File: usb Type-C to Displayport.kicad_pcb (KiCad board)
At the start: 4 copper layers, 50 x 25.9 mm, 23 parts, among them CN1 HYC16-DP20-178, J1 USB_C_Receptacle, U1 VL103-Q3, U2 W25Q16BVSSIG

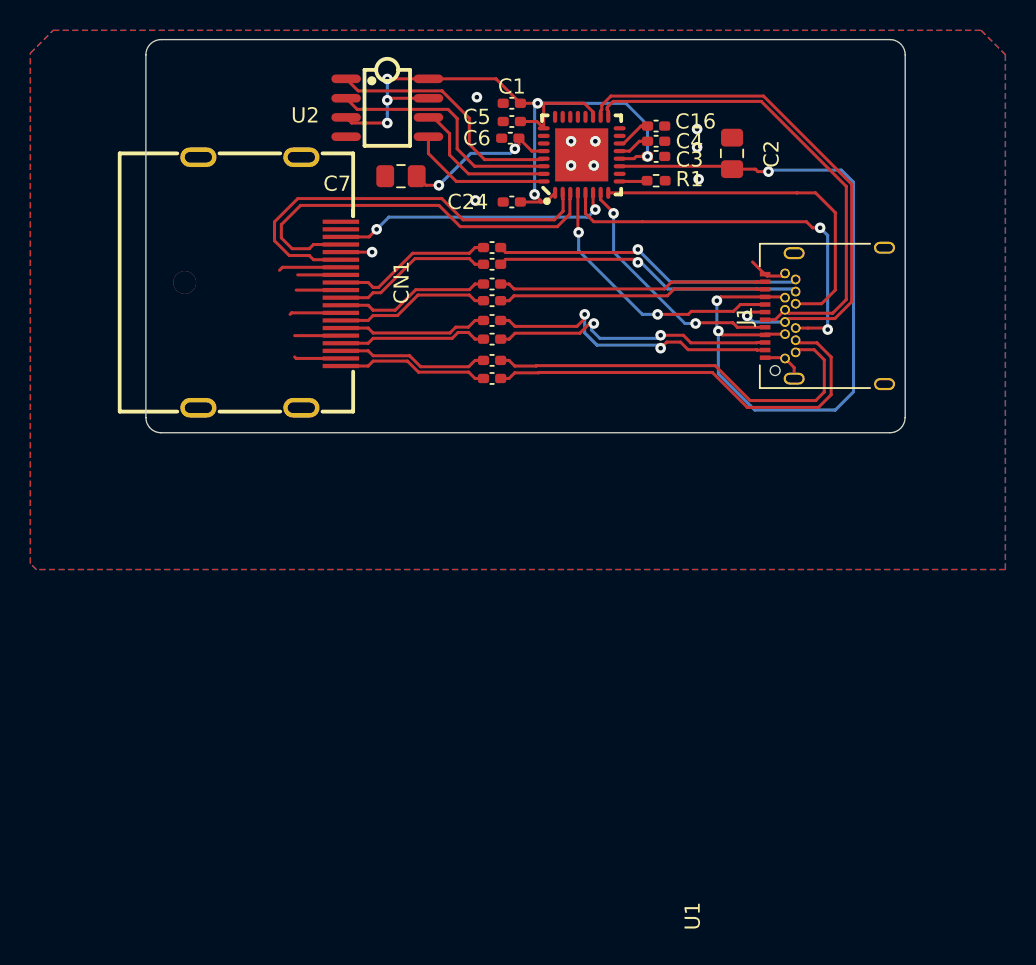
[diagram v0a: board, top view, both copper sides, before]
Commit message: 0.2
Removed SPI chip, fixed CC lines being reversed, made pcb smaller, added mounting holes
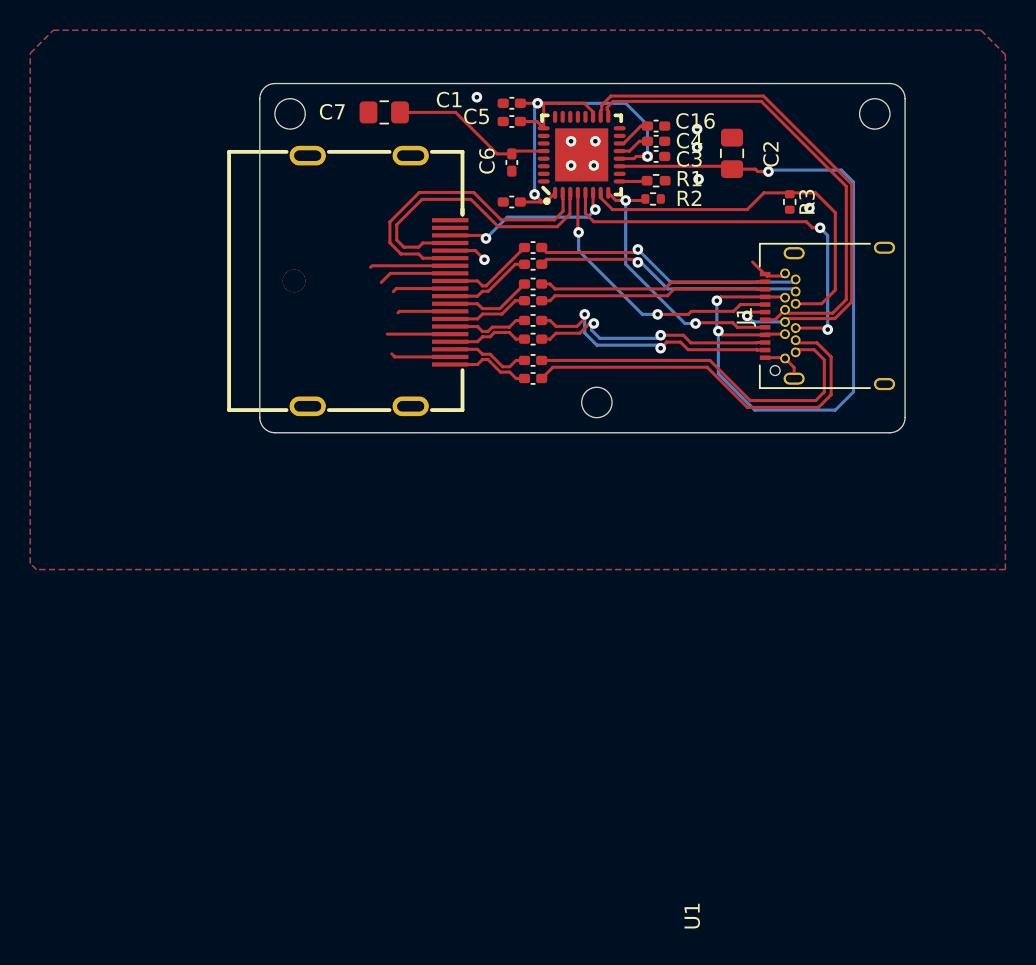
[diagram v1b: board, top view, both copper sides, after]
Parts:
- removed U2: W25Q16BVSSIG, da:SOIC-8_L5.0-W4.0-P1.27-LS6.0-BL
- added R2: 5.1K, Resistor_SMD:R_0402_1005Metric, F.Cu at (103.7, 59.3)
- added R3: 5.1K, Resistor_SMD:R_0402_1005Metric, F.Cu at (112.7, 59.5)
- R1: value 20.5k -> 243K
- moved CN1 7.20 mm to (85.7, 64.7)
- moved C7 4.34 mm to (86.0, 53.6)
- moved C10 2.70 mm to (95.8, 68.5)
- moved C11 2.70 mm to (95.8, 67.3)
- moved C12 2.70 mm to (95.8, 66.0)
- moved C13 2.70 mm to (95.8, 64.9)
- moved C14 2.70 mm to (95.8, 63.6)
- moved C15 2.70 mm to (95.8, 62.5)
- moved C8 2.70 mm to (95.8, 71.1)
- moved C9 2.70 mm to (95.8, 69.9)
- moved G*** 2.15 mm to (108.2, 55.1)
- moved C6 1.60 mm to (94.4, 56.9), turned to -90 degrees
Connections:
- U1 pad 29: SPI_CS -> unconnected-(U1-SPI_CS_-Pad29)
- U1 pad 30: SPI_DO -> unconnected-(U1-SPI_Q-Pad30)
- U1 pad 31: SCLK -> unconnected-(U1-SPI_CLK-Pad31)
- U1 pad 32: SPI_DI -> unconnected-(U1-SPI_D-Pad32)
- U1 pad 7: CC1 -> CC2
- U1 pad 8: CC2 -> CC1
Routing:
- net +3.3V: track 47.7 -> 29.8 mm, vias 6 -> 3
- net SPI_CS: track 16.2 -> 0.00 mm
- net SPI_DO: track 16.0 -> 0.00 mm
- net SCLK: track 9.95 -> 0.00 mm
- net SPI_DI: track 9.46 -> 0.00 mm
- net AUX-: track 27.1 -> 19.4 mm
- net AUX+: track 27.8 -> 20.2 mm
- net HPD: track 18.7 -> 11.6 mm
- net GND: track 27.0 -> 33.4 mm
- net DP_LANE3-: track 10.6 -> 5.76 mm
- net DP_LANE2-: track 10.2 -> 5.39 mm
- net DP_LANE3+: track 10.6 -> 6.07 mm
- net DP_LANE1+: track 9.87 -> 5.32 mm
- net DP_LANE2+: track 10.2 -> 5.70 mm
- net DP_LANE1-: track 9.87 -> 5.32 mm
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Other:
- board size 50 x 25.9 mm -> 42.5 x 23 mm

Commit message: Changed IC to vl100 q3
Changed ic to vl100 q3 (i found it cheaper and it's pin compatible, added Crystal)
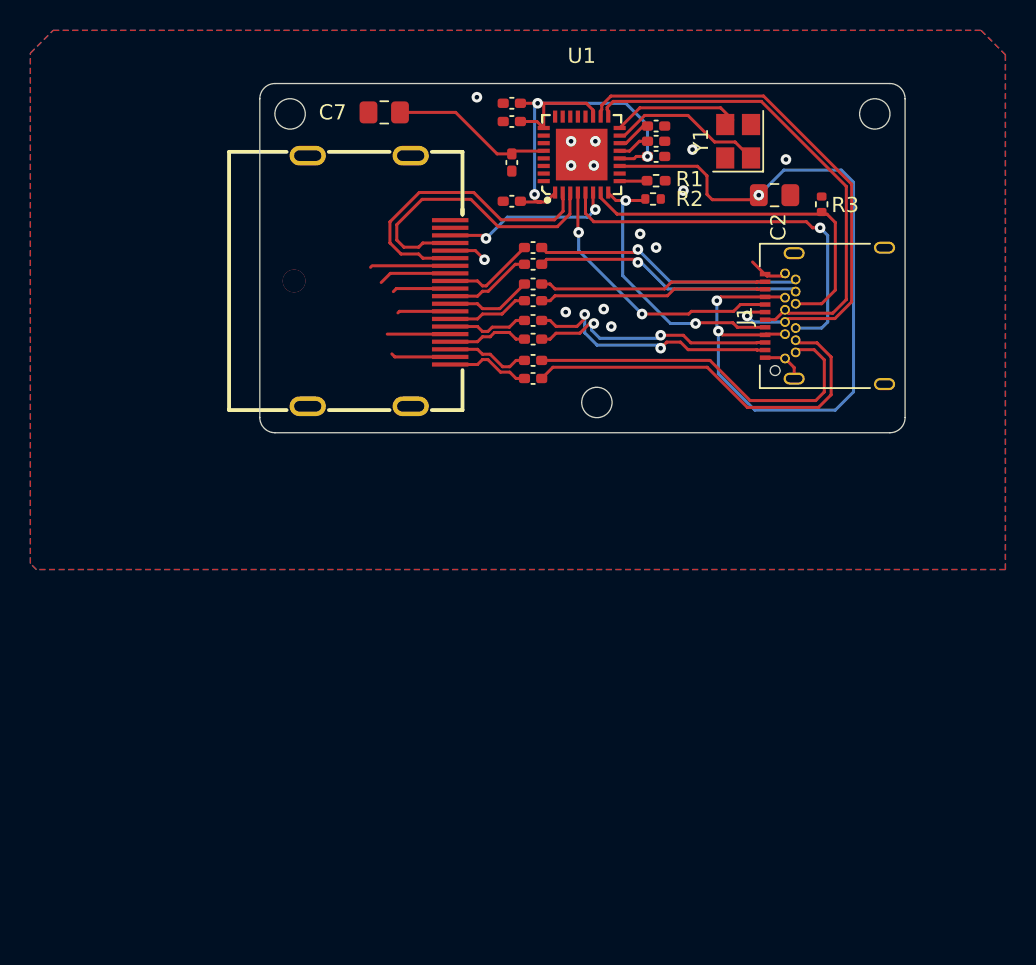
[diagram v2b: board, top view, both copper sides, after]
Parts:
- removed C24: 100nF, Capacitor_SMD:C_0402_1005Metric_Pad0.74x0.62mm_HandSolder
- added C17: 100nF, Capacitor_SMD:C_0402_1005Metric_Pad0.74x0.62mm_HandSolder, F.Cu at (94.4, 59.5)
- added Y1: Crystal_GND24, Crystal:Crystal_SMD_3225-4Pin_3.2x2.5mm, F.Cu at (109.3, 55.5)
- R1: value 243K -> 20.5K
- U1: value VL103-Q3 -> VL100-Q3; footprint da:QFN-32_L5.0-W5.0-P0.50-TL-EP3.5 -> da:QFN-32_L5.0-W5.0-P0.50-BL-EP3.4
- moved C2 3.92 mm to (111.7, 59.0), turned to 0 degrees
- moved R3 2.11 mm to (114.8, 59.6), turned to 90 degrees
- moved G*** 1.10 mm to (107.1, 55.2)
- turned U1 to 0 degrees
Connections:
- U1 pad 15: unconnected-(U1-GPIO11-Pad15) -> Net-(U1-OSCXI)
- U1 pad 16: unconnected-(U1-GPIO10-Pad16) -> Net-(U1-OSCXO)
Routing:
- net Net-(U1-OSCXI): track 0.00 -> 10.4 mm
- net Net-(U1-OSCXO): track 0.00 -> 8.33 mm
- net VBUS: track 54.1 -> 56.3 mm
- net CC2: track 25.2 -> 23.9 mm
- net CC1: track 17.8 -> 18.6 mm
- net SBU2: track 26.3 -> 25.9 mm, vias 2 -> 1
- net GND: vias 10 -> 14

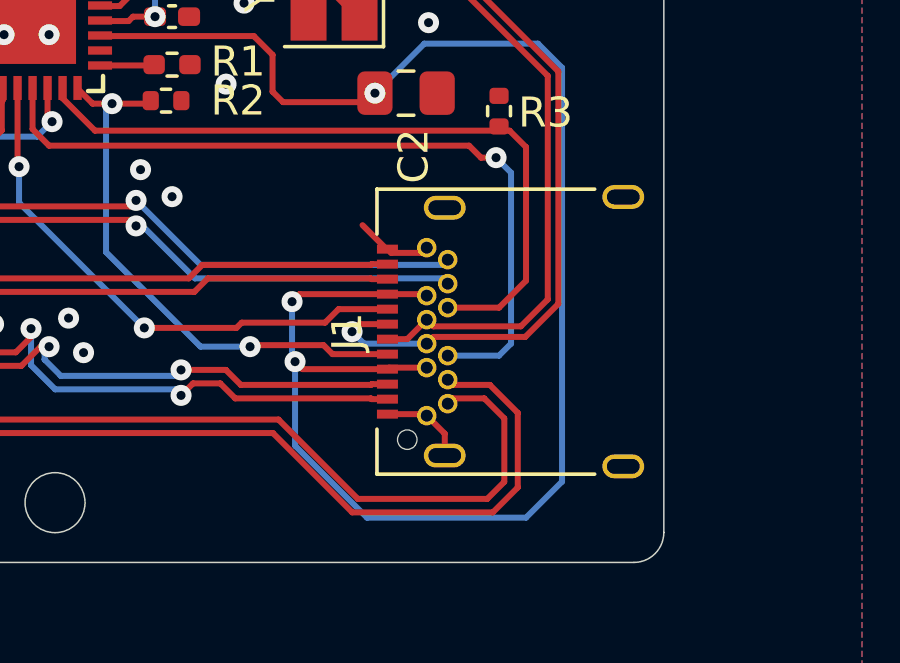
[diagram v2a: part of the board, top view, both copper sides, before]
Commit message: Fixed usb footprint
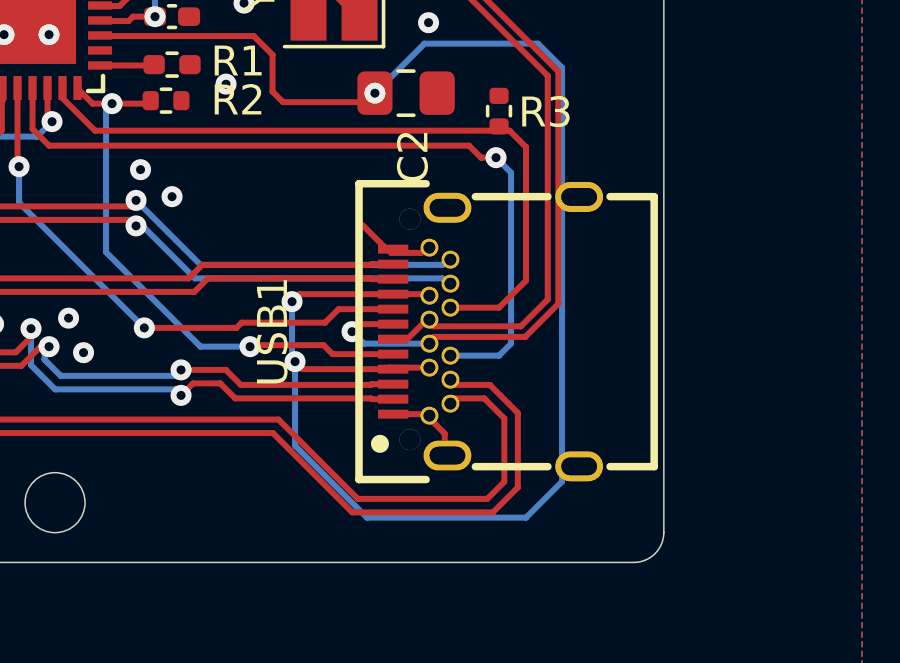
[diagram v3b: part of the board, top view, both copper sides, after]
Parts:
- removed J1: USB_C_Receptacle, Connector_USB:USB_C_Receptacle_Amphenol_12401548E4-2A
- added USB1: TYPEC-324-BCP24, da:USB-C-SMD_TYPEC-324-BCP24, F.Cu at (114.4, 67.0)
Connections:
- C10 pad 1: /TX1- -> TX1-
- C11 pad 1: /TX1+ -> TX1+
- C12 pad 1: /RX2- -> RX2-
- C13 pad 1: /RX2+ -> RX2+
- C14 pad 1: /TX2- -> TX2-
- C15 pad 1: /TX2+ -> TX2+
- C8 pad 1: /RX1- -> RX1-
- C9 pad 1: /RX1+ -> RX1+
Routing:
- net RX1-: track 0.00 -> 26.1 mm
- net /RX1-: track 26.1 -> 0.00 mm
- net RX1+: track 0.00 -> 24.3 mm
- net /RX1+: track 24.3 -> 0.00 mm
- net TX2+: track 0.00 -> 17.9 mm, vias 0 -> 1
- net /TX2+: track 17.9 -> 0.00 mm, vias 1 -> 0
- net TX2-: track 0.00 -> 17.7 mm, vias 0 -> 1
- net /TX2-: track 17.7 -> 0.00 mm, vias 1 -> 0
- net TX1+: track 0.00 -> 17.4 mm, vias 0 -> 2
- net /TX1+: track 17.4 -> 0.00 mm, vias 2 -> 0
- net TX1-: track 0.00 -> 16.3 mm, vias 0 -> 2
- net /TX1-: track 16.3 -> 0.00 mm, vias 2 -> 0
- net RX2-: track 0.00 -> 15.0 mm
- net /RX2-: track 15.0 -> 0.00 mm
- net RX2+: track 0.00 -> 15.0 mm
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
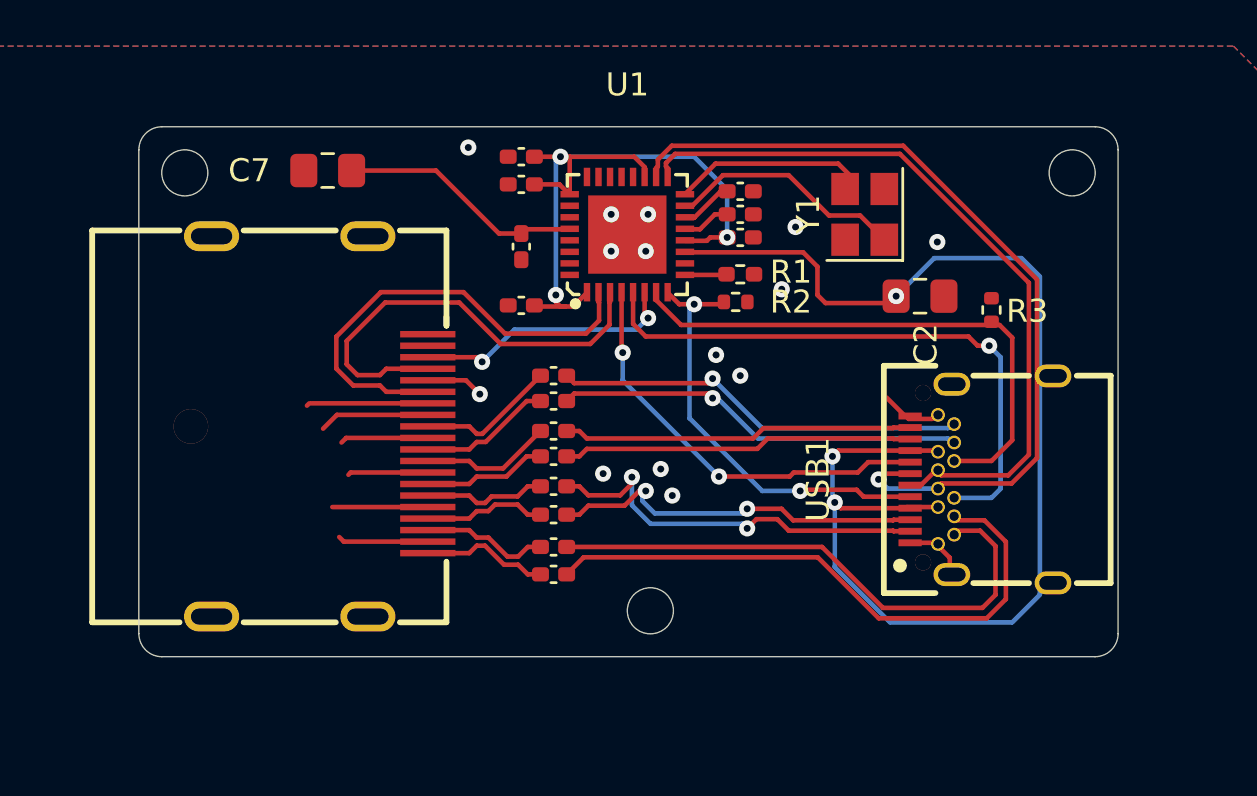
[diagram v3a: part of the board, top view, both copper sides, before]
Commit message: Fixed DP lines
Fixed wrong USB lines to DP lines, fixed differential pairs not length matched, length matched all 4 pairs
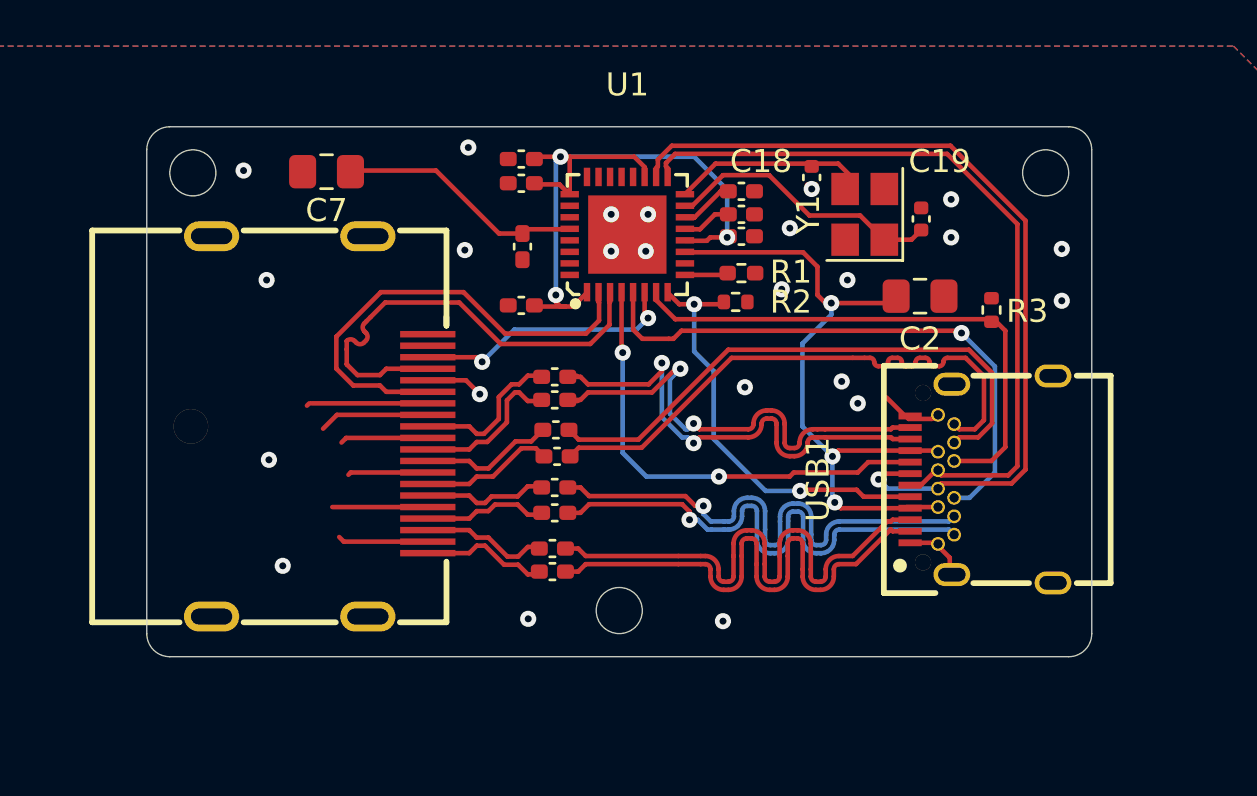
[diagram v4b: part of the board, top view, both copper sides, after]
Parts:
- added C18: 20pF, Capacitor_SMD:C_0402_1005Metric, F.Cu at (107.0, 53.9)
- added C19: 20pF, Capacitor_SMD:C_0402_1005Metric, F.Cu at (111.8, 55.7)
- Y1: value Crystal_GND24 -> 24Mhz
- moved G*** 1.61 mm to (105.5, 54.9)
- moved C10 1.18 mm to (95.8, 67.3)
- moved C12 1.15 mm to (95.9, 64.8)
- moved C11 1.15 mm to (95.8, 68.5)
- moved C8 1.12 mm to (95.8, 70.0)
- moved C13 1.11 mm to (96.0, 66.0)
- moved C9 1.07 mm to (95.8, 71.0)
- moved C14 1.05 mm to (95.8, 62.5)
- moved C15 1.05 mm to (95.8, 63.5)
- moved C1 0.10 mm to (94.4, 53.1)
- moved R1 0.07 mm to (104.0, 58.0)
- moved C3 0.07 mm to (104.0, 56.5)
- moved C7 0.07 mm to (86.0, 53.6)
- moved C5 0.05 mm to (94.4, 54.1)
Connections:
- C10 pad 1: TX1- -> RX1-
- C11 pad 1: TX1+ -> RX1+
- C12 pad 1: RX2- -> TX2-
- C13 pad 1: RX2+ -> TX2+
- C14 pad 1: TX2- -> RX2-
- C15 pad 1: TX2+ -> RX2+
- C8 pad 1: RX1- -> TX1-
- C9 pad 1: RX1+ -> TX1+
- CN1 pad 1: DP_LANE0- -> DP_LANE0+
- CN1 pad 10: DP_LANE3- -> DP_LANE3+
- CN1 pad 12: DP_LANE3+ -> DP_LANE3-
- CN1 pad 3: DP_LANE0+ -> DP_LANE0-
- CN1 pad 4: DP_LANE1- -> DP_LANE1+
- CN1 pad 6: DP_LANE1+ -> DP_LANE1-
- CN1 pad 7: DP_LANE2- -> DP_LANE2+
- CN1 pad 9: DP_LANE2+ -> DP_LANE2-
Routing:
- net VBUS: track 56.3 -> 29.8 mm
- net TX1-: track 16.3 -> 24.6 mm, vias 2 -> 0
- net TX1+: track 17.4 -> 24.6 mm, vias 2 -> 0
- net TX2-: track 17.7 -> 24.7 mm, vias 1 -> 0
- net TX2+: track 17.9 -> 24.7 mm, vias 1 -> 0
- net RX2+: track 15.0 -> 21.1 mm, vias 0 -> 2
- net RX2-: track 15.0 -> 21.1 mm, vias 0 -> 2
- net RX1-: track 26.1 -> 23.5 mm, vias 0 -> 1
- net SBU1: track 18.1 -> 19.9 mm
- net Net-(U1-OSCXI): track 10.4 -> 12.1 mm
- net DP_LANE3-: track 5.76 -> 6.63 mm
- net D-: track 36.5 -> 37.3 mm
- net D+: track 32.4 -> 33.2 mm
- net SBU2: track 25.9 -> 25.1 mm
- net RX1+: track 24.3 -> 23.5 mm, vias 0 -> 1
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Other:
- board size 42.5 x 23 mm -> 41 x 23 mm
- board text added: "USB Type C to DisplayPort (DP Alt Mode)"
- board text removed: "USB Type C to DisplayPort"

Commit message: update
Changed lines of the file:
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@@
 	)
 	(gr_line
-		(start 118.15 74.692893)
-		(end 79.15 74.692893)
+		(start 118.15 74.7)
+		(end 79.15 74.7)
 		(stroke
 			(width 0.05)
@@
 	)
 	(gr_arc
-		(start 79.15 74.692893)
-		(mid 78.44289 74.400003)
-		(end 78.15 73.692893)
+		(start 79.15 74.7)
+		(mid 78.442896 74.407106)
+		(end 78.15 73.7)
 		(stroke
 			(width 0.05)
@@
 	)
 	(gr_circle
-		(center 98.65 72.69)
-		(end 99.65 72.69)
+		(center 98.65 72.7)
+		(end 99.65 72.7)
 		(stroke
 			(width 0.05)
@@
 	)
 	(gr_arc
-		(start 119.15 73.692891)
-		(mid 118.857109 74.4)
-		(end 118.15 74.692891)
+		(start 119.15 73.7)
+		(mid 118.85711 74.407113)
+		(end 118.15 74.7)
 		(stroke
 			(width 0.05)
@@
 	)
 	(gr_line
-		(start 78.15 73.692893)
-		(end 78.15 52.692893)
+		(start 78.15 52.7)
+		(end 78.15 73.7)
 		(stroke
 			(width 0.05)
@@
 	)
 	(via
-		(at 83.45 66.15)
-		(size 0.7)
-		(drill 0.3)
+		(at 80.98 67.71)
+		(size 0.7)
+		(drill 0.3)
